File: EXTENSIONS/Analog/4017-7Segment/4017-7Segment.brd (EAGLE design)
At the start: 48 x 38 mm, 5 parts

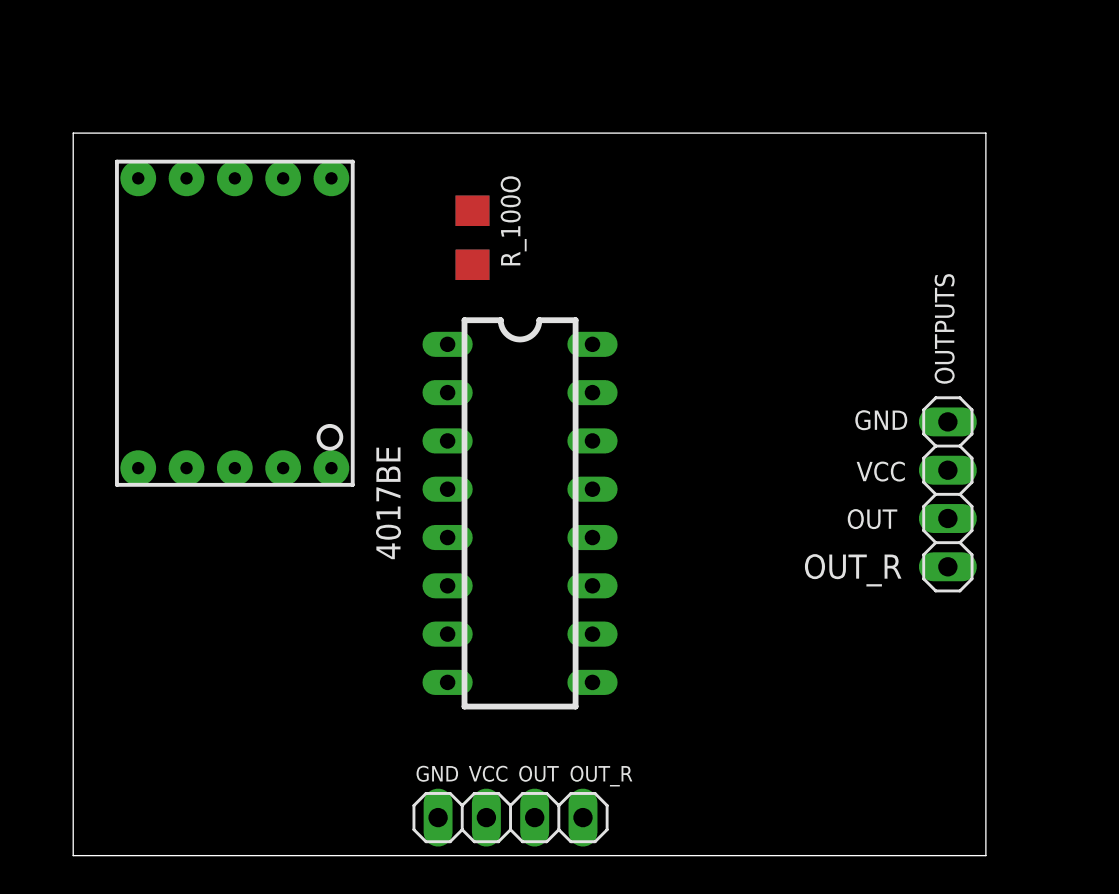
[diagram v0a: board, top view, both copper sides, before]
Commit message: Create UpTo11 Front Panel
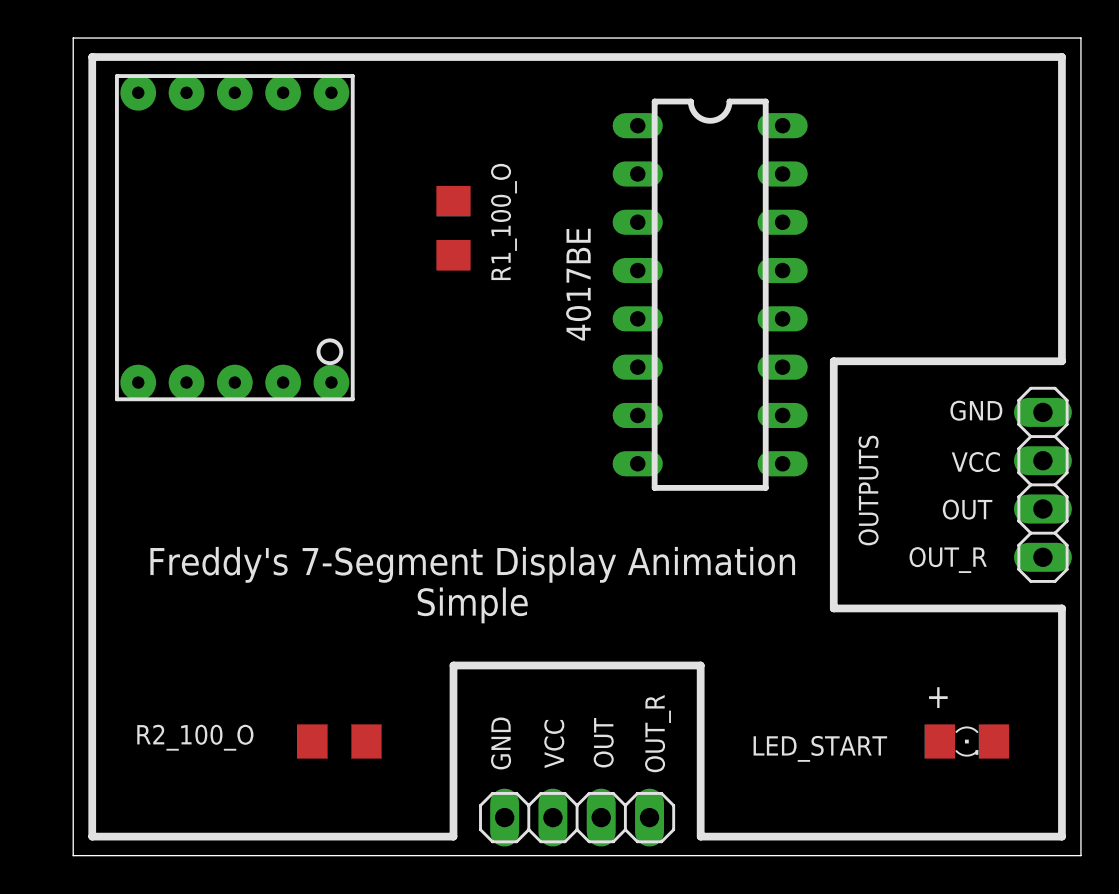
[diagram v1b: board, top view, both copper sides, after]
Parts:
- removed R_100O: (no value), adafruit:R1206
- added LED_START: (no value), adafruit:1206
- added R1_100_O, R2_100_O: (no value), adafruit:R1206
- moved 4017BE 15.2 mm to (35.5, 41.5)
- moved OUTPUTS 5.02 mm to (53.0, 31.5)
- moved U$1 4.50 mm to (10.5, 44.5)
- moved JP_CLOCK_IN 3.50 mm to (28.5, 14.0)
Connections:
- new net N$1: LED_START.C, R2_100_O.2
- net GND: now also R1_100_O.1, R2_100_O.1; no longer R_100O.1
- net N$2: now also R1_100_O.2; no longer R_100O.2
- net SEG_A: now also LED_START.A
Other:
- board size 48 x 38 mm -> 53 x 43 mm
- board text added: "+"
- board text added: "Freddy's 7-Segment Display Animation Simple"
- board text added: "https://bit.ly/36Fu0YN"

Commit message: Create new clock module SMD
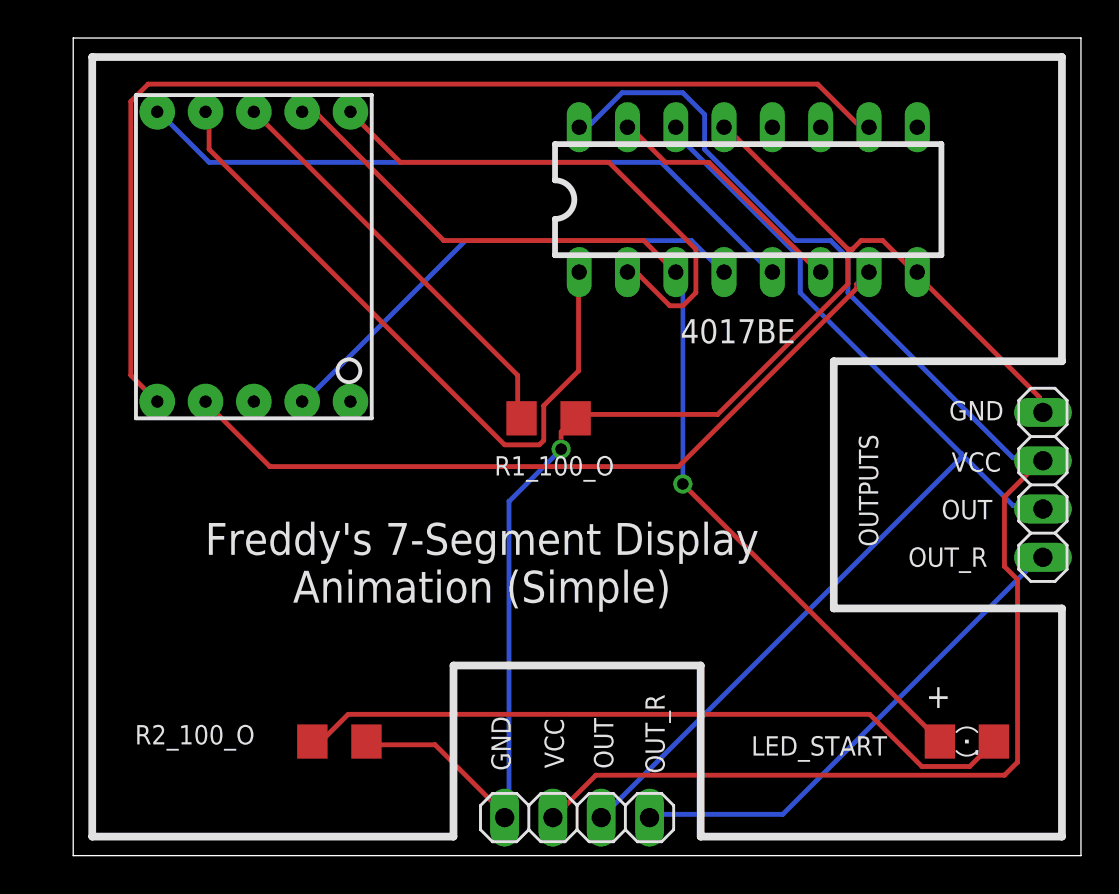
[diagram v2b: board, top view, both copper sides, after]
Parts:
- moved R1_100_O 11.2 mm to (27.0, 35.0), turned to 180 degrees
- moved 4017BE 5.39 mm to (37.5, 46.5), turned to 0 degrees
- moved U$1 1.41 mm to (11.5, 43.5)
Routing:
- net VCC: track 0.00 -> 78.0 mm
- net GND: track 0.00 -> 74.6 mm, vias 0 -> 1
- net SEG_E: track 0.00 -> 56.5 mm
- net TMR555_OUTPUT: track 0.00 -> 55.9 mm
- net SEG_A: track 0.00 -> 53.6 mm, vias 0 -> 1
- net SEG_D: track 0.00 -> 40.7 mm
- net N$1: track 0.00 -> 38.1 mm
- net SEG_F: track 0.00 -> 35.8 mm
- net SEG_G: track 0.00 -> 35.8 mm
- net SEG_B: track 0.00 -> 28.1 mm
- net SEG_C: track 0.00 -> 26.4 mm
- net TMR555_OUTPUT_REVERSE: track 0.00 -> 26.4 mm
- net N$2: track 0.00 -> 22.0 mm
- net RESET: track 0.00 -> 13.3 mm
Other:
- board text added: "Freddy's 7-Segment Display Animation (Simple)"
- board text removed: "Freddy's 7-Segment Display Animation Simple"

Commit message: Fix bug in 4017-7Segment v2
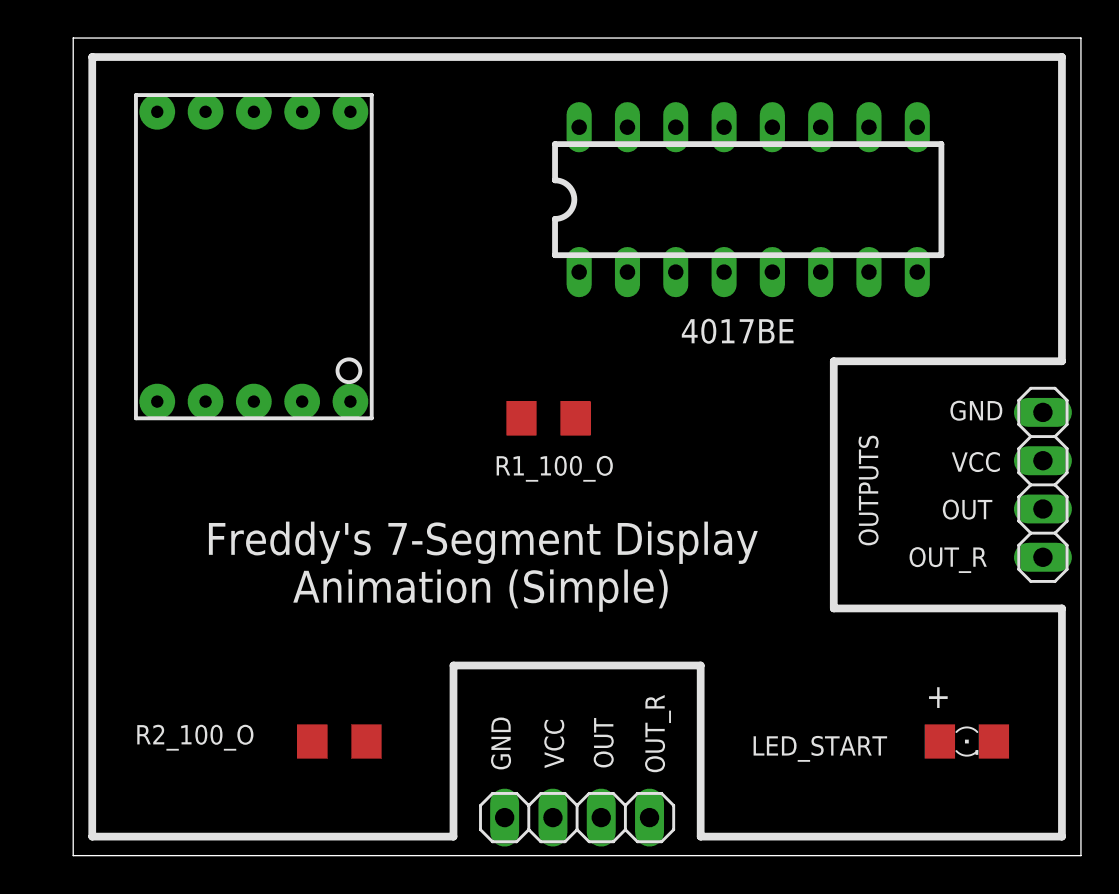
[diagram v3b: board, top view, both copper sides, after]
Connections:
- net RESET: now also 4017BE.5; no longer 4017BE.6
- net SEG_G: no longer 4017BE.5
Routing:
- net VCC: track 78.0 -> 0.00 mm
- net GND: track 74.6 -> 0.00 mm, vias 1 -> 0
- net SEG_E: track 56.5 -> 0.00 mm
- net TMR555_OUTPUT: track 55.9 -> 0.00 mm
- net SEG_A: track 53.6 -> 0.00 mm, vias 1 -> 0
- net SEG_D: track 40.7 -> 0.00 mm
- net N$1: track 38.1 -> 0.00 mm
- net SEG_F: track 35.8 -> 0.00 mm
- net SEG_G: track 35.8 -> 0.00 mm
- net SEG_B: track 28.1 -> 0.00 mm
- net SEG_C: track 26.4 -> 0.00 mm
- net TMR555_OUTPUT_REVERSE: track 26.4 -> 0.00 mm
- net N$2: track 22.0 -> 0.00 mm
- net RESET: track 13.3 -> 0.00 mm

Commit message: Create v2 of Clock de-multiplexer
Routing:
- net GND: track 0.00 -> 80.5 mm
- net VCC: track 0.00 -> 70.8 mm
- net TMR555_OUTPUT: track 0.00 -> 64.8 mm
- net SEG_A: track 0.00 -> 62.3 mm, vias 0 -> 1
- net SEG_E: track 0.00 -> 43.4 mm
- net SEG_D: track 0.00 -> 38.8 mm
- net N$1: track 0.00 -> 37.0 mm
- net SEG_F: track 0.00 -> 35.8 mm
- net SEG_C: track 0.00 -> 26.4 mm
- net TMR555_OUTPUT_REVERSE: track 0.00 -> 26.4 mm
- net N$2: track 0.00 -> 22.0 mm
- net SEG_B: track 0.00 -> 18.1 mm
- net RESET: track 0.00 -> 10.9 mm
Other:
- board text added: "PCBv3 - 2019.12 - Fixed"
- board text removed: "PCBv2 - 2019.12"

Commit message: CReate CheetahBooster
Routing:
- net GND: track 80.5 -> 0.00 mm
- net VCC: track 70.8 -> 0.00 mm
- net TMR555_OUTPUT: track 64.8 -> 0.00 mm
- net SEG_A: track 62.3 -> 0.00 mm, vias 1 -> 0
- net SEG_E: track 43.4 -> 0.00 mm
- net SEG_D: track 38.8 -> 0.00 mm
- net N$1: track 37.0 -> 0.00 mm
- net SEG_F: track 35.8 -> 0.00 mm
- net SEG_C: track 26.4 -> 0.00 mm
- net TMR555_OUTPUT_REVERSE: track 26.4 -> 0.00 mm
- net N$2: track 22.0 -> 0.00 mm
- net SEG_B: track 18.1 -> 0.00 mm
- net RESET: track 10.9 -> 0.00 mm
